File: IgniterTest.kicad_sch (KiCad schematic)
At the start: 19 parts

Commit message: ollie fuckup
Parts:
- removed Fuel_Tank_Pressure1: ~, symbol PID_symbols:Pressure_Transducer
- added PT1: ~, symbol PID:Pressure_Transducer
- added nO_Sol2: ~, symbol PID:Normally Open Solenoid
- renumbered PT1 to PT2, PT2 to PT3, PT3 to PT4, PT4 to PT5, PT5 to PT6
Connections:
- net at Torch_Ignitor1.: now also nO_Sol2.
- net at Fuel_Main_Servo1.: now also CV2.; no longer Fuel_Tank1.
- net at N2_Bottle1.: now also N2_Reg1.
- net at PT4.: now also CV1., nO_Sol2.
- net at CV1.: now also Ox_Main_Servo1.; no longer PT4.
- net at N2O_Bottle1.: now also Reg1.
- net at Reg1.: now also Ox_Main_Servo1., PT3.; no longer N2O_Bottle1.
- new net: Fuel_Press1., N2_Reg1., Needle_Valve1., PT1.
- new net: CV2., PT5., Torch_Ignitor1.
- new net: Fuel_Main_Servo1., Fuel_Tank1.
- now unconnected: Needle_Valve1., PT3., PT5.
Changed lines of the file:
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@@
+	(wire
+		(pts
+			(xy 129.54 71.12) (xy 134.62 71.12)
+		)
+		(stroke
+			(width 0)
+			(type default)
+		)
+	)
 	(wire
 		(pts
@@
 	(wire
 		(pts
-			(xy 129.54 71.12) (xy 134.62 71.12)
-		)
-		(stroke
-			(width 0)
-			(type default)
-		)
-	)
-	(wire
-		(pts
 			(xy 109.22 132.08) (xy 109.22 130.81)
 		)
@@
 	(wire
 		(pts
+			(xy 134.62 71.12) (xy 134.62 73.66)
+		)
+		(stroke
+			(width 0)
+			(type default)
+		)
+	)
+	(wire
+		(pts
 			(xy 133.35 153.67) (xy 133.35 157.48)
 		)
@@
 	(wire
 		(pts
-			(xy 134.62 71.12) (xy 134.62 73.66)
-		)
-		(stroke
-			(width 0)
-			(type default)
-		)
-	)
-	(wire
-		(pts
 			(xy 109.22 101.6) (xy 109.22 104.14)
 		)
@@
 			(width 0)
 			(type default)
+		)
+	)
+	(symbol
+		(lib_name "PID:Pressure_Transducer")
+		(lib_id "PID:Pressure_Transducer")
+		(at 127 71.12 0)
+		(unit 1)
+		(exclude_from_sim no)
+		(in_bom yes)
+		(on_board yes)
+		(dnp no)
+		(fields_autoplaced yes)
+		(property "Reference" "PT1"
+			(at 127 66.04 0)
+			(effects
+				(font
+					(size 1.27 1.27)
+				)
+			)
+		)
+		(property "Value" "~"
+			(at 127 72.39 0)
+			(effects
+				(font
+					(size 1.27 1.27)
+				)
+				(hide yes)
+			)
+		)
+		(property "Footprint" ""
+			(at 127 71.12 0)
+			(effects
+				(font
+					(size 1.27 1.27)
+				)
+				(hide yes)
+			)
+		)
+		(property "Datasheet" ""
+			(at 127 71.12 0)
+			(effects
+				(font
+					(size 1.27 1.27)
+				)
+				(hide yes)
+			)
+		)
+		(property "Description" ""
+			(at 127 71.12 0)
+			(effects
+				(font
+					(size 1.27 1.27)
+				)
+				(hide yes)
+			)
+		)
+		(pin ""
+		)
+		(pin ""
+		)
+		(pin ""
+		)
+		(instances
+			(project ""
+				(path "/045f1f05-3134-4b6d-91b6-463031104f1e/6a55bbd5-ed21-4b79-a194-d378f68dea1b"
+					(reference "PT1")
+					(unit 1)
+				)
+			)
 		)
 	)
@@
 	)
 	(symbol
+		(lib_name "PID_symbols:Pressure_Transducer")
 		(lib_id "PID_symbols:Pressure_Transducer")
 		(at 139.7 157.48 0)
@@
 		(on_board yes)
 		(dnp no)
-		(property "Reference" "PT5"
+		(property "Reference" "PT6"
 			(at 139.7 161.29 0)
 			(effects
@@
 			(project "P_IDs"
 				(path "/045f1f05-3134-4b6d-91b6-463031104f1e/6a55bbd5-ed21-4b79-a194-d378f68dea1b"
-					(reference "PT5")
+					(reference "PT6")
 					(unit 1)
 				)
@@
 	)
 	(symbol
-		(lib_name "PID_symbols:Pressure_Transducer")
-		(lib_id "PID_symbols:Pressure_Transducer")
-		(at 127 71.12 0)
-		(unit 1)
-		(exclude_from_sim no)
-		(in_bom yes)
-		(on_board yes)
-		(dnp no)
-		(property "Reference" "Fuel_Tank_Pressure1"
-			(at 127 74.93 0)
-			(effects
-				(font
-					(size 1.27 1.27)
-				)
-			)
-		)
-		(property "Value" "~"
-			(at 127 72.39 0)
-			(effects
-				(font
-					(size 1.27 1.27)
-				)
-				(hide yes)
-			)
-		)
-		(property "Footprint" ""
-			(at 127 71.12 0)
-			(effects
-				(font
-					(size 1.27 1.27)
-				)
-				(hide yes)
-			)
-		)
-		(property "Datasheet" ""
-			(at 127 71.12 0)
-			(effects
-				(font
-					(size 1.27 1.27)
-				)
-				(hide yes)
-			)
-		)
-		(property "Description" ""
-			(at 127 71.12 0)
-			(effects
-				(font
-					(size 1.27 1.27)
-				)
-				(hide yes)
-			)
-		)
-		(pin ""
-		)
-		(pin ""
-		)
-		(pin ""
-		)
-		(instances
-			(project "P_IDs"
-				(path "/045f1f05-3134-4b6d-91b6-463031104f1e/6a55bbd5-ed21-4b79-a194-d378f68dea1b"
-					(reference "Fuel_Tank_Pressure1")
-					(unit 1)
-				)
-			)
-		)
-	)
-	(symbol
 		(lib_id "PID_symbols:Needle_Valve")
 		(at 151.13 71.12 0)
@@
 	)
 	(symbol
+		(lib_name "PnID_symbols:Tank")
 		(lib_id "PnID_symbols:Tank")
 		(at 133.35 52.07 0)
@@
 	)
 	(symbol
+		(lib_name "PnID_symbols:Tank")
 		(lib_id "PnID_symbols:Tank")
 		(at 133.35 105.41 0)
@@
 	)
 	(symbol
+		(lib_name "PID_symbols:Pressure_Transducer")
 		(lib_id "PID_symbols:Pressure_Transducer")
 		(at 139.7 149.86 0)
@@
 		(on_board yes)
 		(dnp no)
-		(property "Reference" "PT4"
+		(property "Reference" "PT5"
 			(at 139.7 153.67 0)
 			(effects
@@
 			(project "P_IDs"
 				(path "/045f1f05-3134-4b6d-91b6-463031104f1e/6a55bbd5-ed21-4b79-a194-d378f68dea1b"
-					(reference "PT4")
+					(reference "PT5")
 					(unit 1)
 				)
@@
 	)
 	(symbol
+		(lib_name "PID_symbols:Pressure_Transducer")
 		(lib_id "PID_symbols:Pressure_Transducer")
 		(at 100.33 132.08 0)
@@
 		(on_board yes)
 		(dnp no)
-		(property "Reference" "PT3"
+		(property "Reference" "PT4"
 			(at 100.33 135.89 0)
 			(effects
@@
 			(project "P_IDs"
 				(path "/045f1f05-3134-4b6d-91b6-463031104f1e/6a55bbd5-ed21-4b79-a194-d378f68dea1b"
-					(reference "PT3")
+					(reference "PT4")
 					(unit 1)
 				)
@@
 	)
 	(symbol
+		(lib_name "PnID_symbols:Tank")
 		(lib_id "PnID_symbols:Tank")
 		(at 107.95 82.55 0)
@@
 	)
 	(symbol
+		(lib_name "PID_symbols:Check_Valve")
 		(lib_id "PID_symbols:Check_Valve")
 		(at 109.22 123.19 270)
@@
 	)
 	(symbol
+		(lib_name "PID:Normally Open Solenoid")
+		(lib_id "PID:Normally Open Solenoid")
+		(at 109.22 134.62 270)
+		(unit 1)
+		(exclude_from_sim no)
+		(in_bom yes)
+		(on_board yes)
+		(dnp no)
+		(fields_autoplaced yes)
+		(property "Reference" "nO_Sol2"
+			(at 115.57 137.7949 90)
+			(effects
+				(font
+					(size 1.27 1.27)
+				)
+				(justify left)
+			)
+		)
+		(property "Value" "~"
+			(at 115.57 139.7 90)
+			(effects
+				(font
+					(size 1.27 1.27)
+				)
+				(justify left)
+			)
+		)
+		(property "Footprint" ""
+			(at 109.22 134.62 0)
+			(effects
+				(font
+					(size 1.27 1.27)
+				)
+				(hide yes)
+			)
+		)
+		(property "Datasheet" ""
+			(at 109.22 134.62 0)
+			(effects
+				(font
+					(size 1.27 1.27)
+				)
+				(hide yes)
+			)
+		)
+		(property "Description" ""
+			(at 109.22 134.62 0)
+			(effects
+				(font
+					(size 1.27 1.27)
+				)
+				(hide yes)
+			)
+		)
+		(pin ""
+		)
+		(pin ""
+		)
+		(instances
+			(project ""
+				(path "/045f1f05-3134-4b6d-91b6-463031104f1e/6a55bbd5-ed21-4b79-a194-d378f68dea1b"
+					(reference "nO_Sol2")
+					(unit 1)
+				)
+			)
+		)
+	)
+	(symbol
+		(lib_name "PID_symbols:Check_Valve")
 		(lib_id "PID_symbols:Check_Valve")
 		(at 134.62 134.62 270)
@@
 	)
 	(symbol
+		(lib_name "PID:Normally Open Solenoid")
 		(lib_id "PID:Normally Open Solenoid")
 		(at 151.13 90.17 0)
@@
 	)
 	(symbol
+		(lib_name "PID_symbols:Pressure_Transducer")
 		(lib_id "PID_symbols:Pressure_Transducer")
 		(at 127 90.17 0)
@@
 		(on_board yes)
 		(dnp no)
-		(property "Reference" "PT1"
+		(property "Reference" "PT2"
 			(at 127 93.98 0)
 			(effects
@@
 			(project "P_IDs"
 				(path "/045f1f05-3134-4b6d-91b6-463031104f1e/6a55bbd5-ed21-4b79-a194-d378f68dea1b"
-					(reference "PT1")
+					(reference "PT2")
 					(unit 1)
 				)
@@
 	)
 	(symbol
+		(lib_name "PID:Pressure_Transducer")
 		(lib_id "PID:Pressure_Transducer")
 		(at 102.87 104.14 0)
@@
 		(dnp no)
 		(fields_autoplaced yes)
-		(property "Reference" "PT2"
+		(property "Reference" "PT3"
 			(at 102.87 99.06 0)
 			(effects
@@
 			(project ""
 				(path "/045f1f05-3134-4b6d-91b6-463031104f1e/6a55bbd5-ed21-4b79-a194-d378f68dea1b"
-					(reference "PT2")
-					(unit 1)
-				)
+					(reference "PT3")
+					(unit 1)
+				)

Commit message: fuckup 2
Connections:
- net at PT1.: now also Fuel_Press1., N2_Reg1., Needle_Valve1.
- net at Fuel_Main_Servo1.: now also CV2.; no longer Fuel_Tank1.
- net at N2_Bottle1.: now also N2_Reg1.
- net at PT4.: now also CV1., nO_Sol2.
- net at N2O_Bottle1.: now also Reg1.
- net at Reg1.: now also Ox_Main_Servo1., PT3.; no longer N2O_Bottle1.
- new net: CV2., PT5., Torch_Ignitor1.
- new net: Fuel_Main_Servo1., Fuel_Tank1.
- now unconnected: Needle_Valve1., PT3., PT5.
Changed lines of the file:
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@@
 	)
 	(symbol
-		(lib_name "PID:Pressure_Transducer")
 		(lib_id "PID:Pressure_Transducer")
 		(at 127 71.12 0)
@@
 	)
 	(symbol
-		(lib_name "PID_symbols:Pressure_Transducer")
 		(lib_id "PID_symbols:Pressure_Transducer")
 		(at 139.7 157.48 0)
@@
 	)
 	(symbol
-		(lib_name "PnID_symbols:Tank")
 		(lib_id "PnID_symbols:Tank")
 		(at 133.35 52.07 0)
@@
 	)
 	(symbol
-		(lib_name "PnID_symbols:Tank")
 		(lib_id "PnID_symbols:Tank")
 		(at 133.35 105.41 0)
@@
 	)
 	(symbol
-		(lib_name "PID_symbols:Pressure_Transducer")
 		(lib_id "PID_symbols:Pressure_Transducer")
 		(at 139.7 149.86 0)
@@
 	)
 	(symbol
-		(lib_name "PID_symbols:Pressure_Transducer")
 		(lib_id "PID_symbols:Pressure_Transducer")
 		(at 100.33 132.08 0)
@@
 	)
 	(symbol
-		(lib_name "PnID_symbols:Tank")
 		(lib_id "PnID_symbols:Tank")
 		(at 107.95 82.55 0)
@@
 	)
 	(symbol
-		(lib_name "PID_symbols:Check_Valve")
 		(lib_id "PID_symbols:Check_Valve")
 		(at 109.22 123.19 270)
@@
 	)
 	(symbol
-		(lib_name "PID:Normally Open Solenoid")
 		(lib_id "PID:Normally Open Solenoid")
 		(at 109.22 134.62 270)
@@
 	)
 	(symbol
-		(lib_name "PID_symbols:Check_Valve")
 		(lib_id "PID_symbols:Check_Valve")
 		(at 134.62 134.62 270)
@@
 	)
 	(symbol
-		(lib_name "PID:Normally Open Solenoid")
 		(lib_id "PID:Normally Open Solenoid")
 		(at 151.13 90.17 0)
@@
 	)
 	(symbol
-		(lib_name "PID_symbols:Pressure_Transducer")
 		(lib_id "PID_symbols:Pressure_Transducer")
 		(at 127 90.17 0)
@@
 	)
 	(symbol
-		(lib_name "PID:Pressure_Transducer")
 		(lib_id "PID:Pressure_Transducer")
 		(at 102.87 104.14 0)

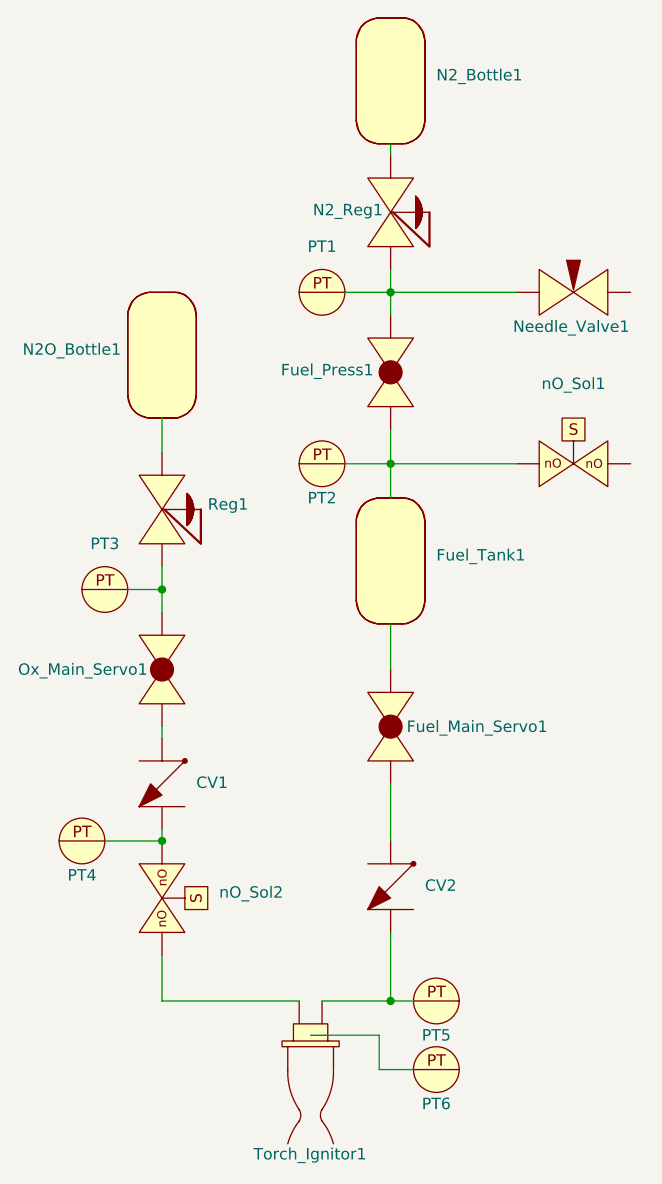
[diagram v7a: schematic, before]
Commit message: Added Igniter + Hopper Engine test
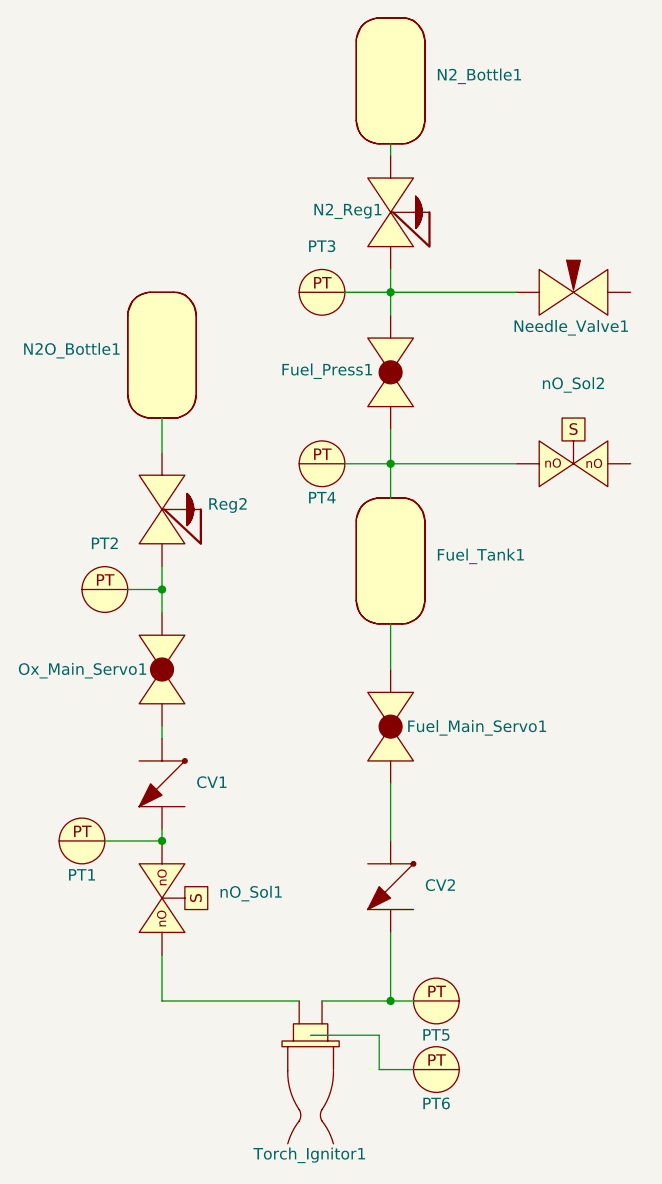
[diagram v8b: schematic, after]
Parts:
- renumbered PT4 to PT1, PT3 to PT2, PT1 to PT3, PT2 to PT4, Reg1 to Reg2, nO_Sol2 to nO_Sol1, nO_Sol1 to nO_Sol2
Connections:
- net at PT3.: now also Fuel_Press1., N2_Reg1., Needle_Valve1.
- net at Fuel_Main_Servo1.: now also CV2.; no longer Fuel_Tank1.
- net at N2_Bottle1.: now also N2_Reg1.
- net at PT1.: now also CV1., nO_Sol1.
- net at N2O_Bottle1.: now also Reg2.
- net at Reg2.: now also Ox_Main_Servo1., PT2.; no longer N2O_Bottle1.
- new net: CV2., PT5., Torch_Ignitor1.
- new net: Fuel_Main_Servo1., Fuel_Tank1.
- now unconnected: Needle_Valve1., PT2., PT5.
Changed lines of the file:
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@@
 		(dnp no)
 		(fields_autoplaced yes)
-		(property "Reference" "PT1"
+		(property "Reference" "PT3"
 			(at 127 66.04 0)
 			(effects
@@
 			(project ""
 				(path "/045f1f05-3134-4b6d-91b6-463031104f1e/6a55bbd5-ed21-4b79-a194-d378f68dea1b"
-					(reference "PT1")
+					(reference "PT3")
 					(unit 1)
 				)
@@
 		(on_board yes)
 		(dnp no)
-		(property "Reference" "PT4"
+		(property "Reference" "PT1"
 			(at 100.33 135.89 0)
 			(effects
@@
 			(project "P_IDs"
 				(path "/045f1f05-3134-4b6d-91b6-463031104f1e/6a55bbd5-ed21-4b79-a194-d378f68dea1b"
-					(reference "PT4")
+					(reference "PT1")
 					(unit 1)
 				)
@@
 		(dnp no)
 		(fields_autoplaced yes)
-		(property "Reference" "Reg1"
+		(property "Reference" "Reg2"
 			(at 114.3 94.6774 90)
 			(effects
@@
 			(project ""
 				(path "/045f1f05-3134-4b6d-91b6-463031104f1e/6a55bbd5-ed21-4b79-a194-d378f68dea1b"
-					(reference "Reg1")
+					(reference "Reg2")
 					(unit 1)
 				)
@@
 		(dnp no)
 		(fields_autoplaced yes)
-		(property "Reference" "nO_Sol2"
+		(property "Reference" "nO_Sol1"
 			(at 115.57 137.7949 90)
 			(effects
@@
 			(project ""
 				(path "/045f1f05-3134-4b6d-91b6-463031104f1e/6a55bbd5-ed21-4b79-a194-d378f68dea1b"
-					(reference "nO_Sol2")
+					(reference "nO_Sol1")
 					(unit 1)
 				)
@@
 		(dnp no)
 		(fields_autoplaced yes)
-		(property "Reference" "nO_Sol1"
+		(property "Reference" "nO_Sol2"
 			(at 154.94 81.28 0)
 			(effects
@@
 			(project ""
 				(path "/045f1f05-3134-4b6d-91b6-463031104f1e/6a55bbd5-ed21-4b79-a194-d378f68dea1b"
-					(reference "nO_Sol1")
+					(reference "nO_Sol2")
 					(unit 1)
 				)
@@
 		(on_board yes)
 		(dnp no)
-		(property "Reference" "PT2"
+		(property "Reference" "PT4"
 			(at 127 93.98 0)
 			(effects
@@
 			(project "P_IDs"
 				(path "/045f1f05-3134-4b6d-91b6-463031104f1e/6a55bbd5-ed21-4b79-a194-d378f68dea1b"
-					(reference "PT2")
+					(reference "PT4")
 					(unit 1)
 				)
@@
 		(dnp no)
 		(fields_autoplaced yes)
-		(property "Reference" "PT3"
+		(property "Reference" "PT2"
 			(at 102.87 99.06 0)
 			(effects
@@
 			(project ""
 				(path "/045f1f05-3134-4b6d-91b6-463031104f1e/6a55bbd5-ed21-4b79-a194-d378f68dea1b"
-					(reference "PT3")
-					(unit 1)
-				)
+					(reference "PT2")
+					(unit 1)
+				)
